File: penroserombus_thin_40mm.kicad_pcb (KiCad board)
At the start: 2 copper layers, 72.4 x 23.5 mm, 15 parts, among them J1 Conn_01x03_Female, J2 Conn_01x03_Female, J3 Conn_01x03_Male, J4 Conn_01x03_Male, M2 MountingHole_2.2mm_M2_ISO7380, SW1 SW_DPDT_x2

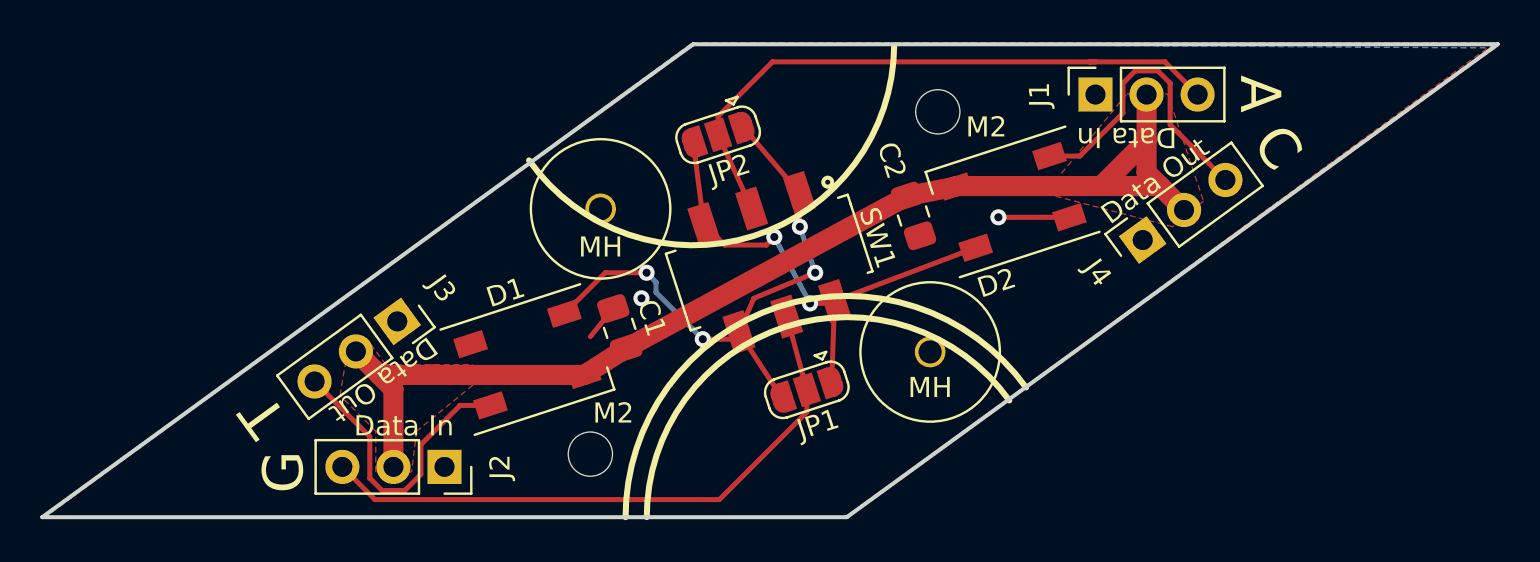
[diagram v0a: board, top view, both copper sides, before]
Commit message: board has 4 leds instead of 2.
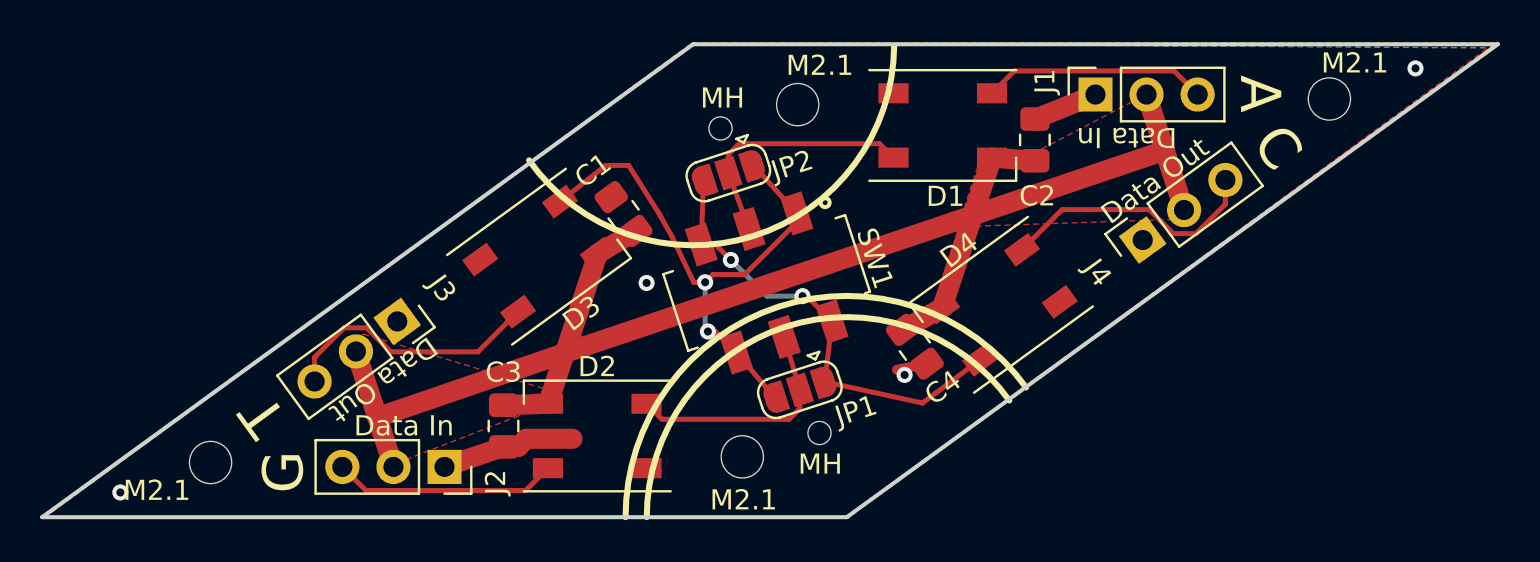
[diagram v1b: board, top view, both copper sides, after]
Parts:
- removed M2 (x2): MountingHole_2.2mm_M2_ISO7380, MountingHole:MountingHole_2.2mm_M2_ISO7380
- removed the MH at (162.9, 76.8)
- removed the MH at (146.6, 69.7)
- added C3: C, Capacitor_SMD:C_0805_2012Metric_Pad1.18x1.45mm_HandSolder, F.Cu at (141.7, 80.5)
- added C4: C, Capacitor_SMD:C_0805_2012Metric_Pad1.18x1.45mm_HandSolder, F.Cu at (162.2, 76.6)
- added D1: SK6812, LED_SMD:LED_SK6812_PLCC4_5.0x5.0mm_P3.2mm, F.Cu at (163.6, 65.6)
- added D2: SK6812, LED_SMD:LED_SK6812_PLCC4_5.0x5.0mm_P3.2mm, F.Cu at (146.4, 81.0)
- added M2.1: MountingHole_2.1mm, MountingHole:MountingHole_2.1mm, F.Cu at (153.6, 82.1)
- added M2.1: MountingHole_2.1mm, MountingHole:MountingHole_2.1mm, F.Cu at (156.4, 64.5)
- added M2.1: MountingHole_2.1mm, MountingHole:MountingHole_2.1mm, F.Cu at (127.2, 82.3)
- added M2.1: MountingHole_2.1mm, MountingHole:MountingHole_2.1mm, F.Cu at (182.8, 64.3)
- added MH: Pushpin_mountinghole, penroserombus:Pushpin_mountinghole, F.Cu at (157.4, 80.9)
- added MH: Pushpin_mountinghole, penroserombus:Pushpin_mountinghole, F.Cu at (152.5, 65.7)
- moved C2 7.12 mm to (168.1, 66.3), turned to 270 degrees
- moved C1 5.69 mm to (147.7, 70.0), turned to 306 degrees
- moved D3 5.15 mm to (143.5, 72.1), turned to 36 degrees
- moved D4 5.15 mm to (166.5, 74.5), turned to 216 degrees
- moved JP2 1.97 mm to (152.9, 67.9)
- moved SW1 1.02 mm to (154.8, 73.4)
- moved JP1 0.35 mm to (156.5, 78.7)
- renumbered D1 to D3, D2 to D4
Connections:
- J1 pad 3: Net-(J1-Pad3) -> Net-(D1-Pad2)
- J2 pad 3: Net-(J2-Pad3) -> Net-(D2-Pad2)
- JP1 pad 2: Net-(J2-Pad3) -> Net-(D2-Pad4)
- JP2 pad 2: Net-(J1-Pad3) -> Net-(D1-Pad4)
- SW1 pad 2: Net-(J1-Pad3) -> Net-(D1-Pad4)
- SW1 pad 5: Net-(J2-Pad3) -> Net-(D2-Pad4)
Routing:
- net Net-(J1-Pad3): track 30.9 -> 0.00 mm
- net Net-(J2-Pad3): track 30.4 -> 0.00 mm
- net VCC: track 57.4 -> 77.9 mm
- net Net-(D1-Pad4): track 0.00 -> 12.6 mm
- net Net-(D2-Pad4): track 0.00 -> 11.8 mm
- net Net-(D1-Pad2): track 0.00 -> 11.2 mm
- net Net-(D2-Pad2): track 0.00 -> 11.2 mm
- net GND: track 5.37 -> 11.5 mm, vias 2 -> 4
- net Net-(D4-Pad2): track 24.9 -> 22.8 mm
- net Net-(D3-Pad4): track 14.9 -> 13.2 mm
- net Net-(D4-Pad4): track 14.8 -> 13.2 mm
- net Net-(D3-Pad2): track 29.2 -> 28.1 mm, vias 4 -> 2

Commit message: small tweaks to traces
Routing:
- net GND: vias 4 -> 11
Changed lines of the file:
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@@
     (thickness 1.6)
     (drawings 31)
-    (tracks 82)
+    (tracks 90)
     (zones 0)
     (modules 21)
@@
       (effects (font (size 0.5 0.5) (thickness 0.08)))
     )
-    (pad 1 smd roundrect (at -1.0375 0 126) (size 1.175 1.45) (layers F.Cu F.Paste F.Mask) (roundrect_rratio 0.212766)
-      (net 2 GND))
-    (pad 2 smd roundrect (at 1.0375 0 126) (size 1.175 1.45) (layers F.Cu F.Paste F.Mask) (roundrect_rratio 0.212766)
+    (pad 1 smd roundrect (at -1.0375 0 126) (size 1.175 1.45) (layers F.Cu F.Paste F.Mask) (roundrect_rratio 0.2127659574468085)
+      (net 2 GND))
+    (pad 2 smd roundrect (at 1.0375 0 126) (size 1.175 1.45) (layers F.Cu F.Paste F.Mask) (roundrect_rratio 0.2127659574468085)
       (net 1 VCC))
     (model ${KISYS3DMOD}/Capacitor_SMD.3dshapes/C_0805_2012Metric.wrl
@@
       (effects (font (size 0.5 0.5) (thickness 0.08)))
     )
-    (pad 2 smd roundrect (at 1.0375 0 90) (size 1.175 1.45) (layers F.Cu F.Paste F.Mask) (roundrect_rratio 0.212766)
-      (net 1 VCC))
-    (pad 1 smd roundrect (at -1.0375 0 90) (size 1.175 1.45) (layers F.Cu F.Paste F.Mask) (roundrect_rratio 0.212766)
+    (pad 2 smd roundrect (at 1.0375 0 90) (size 1.175 1.45) (layers F.Cu F.Paste F.Mask) (roundrect_rratio 0.2127659574468085)
+      (net 1 VCC))
+    (pad 1 smd roundrect (at -1.0375 0 90) (size 1.175 1.45) (layers F.Cu F.Paste F.Mask) (roundrect_rratio 0.2127659574468085)
       (net 2 GND))
     (model ${KISYS3DMOD}/Capacitor_SMD.3dshapes/C_0805_2012Metric.wrl
@@
   (segment (start 142.457 81.5555) (end 142.8595 81.153) (width 1) (layer F.Cu) (net 2))
   (segment (start 141.732 81.5555) (end 142.457 81.5555) (width 1) (layer F.Cu) (net 2))
-  (segment (start 142.8595 81.153) (end 145.161 81.153) (width 1) (layer F.Cu) (net 2))
+  (segment (start 142.8595 81.153) (end 143.129 81.153) (width 1) (layer F.Cu) (net 2))
   (segment (start 138.799045 82.55) (end 141.732 81.5555) (width 1) (layer F.Cu) (net 2))
-  (via (at 161.671 77.978) (size 0.8) (drill 0.4) (layers F.Cu B.Cu) (net 2))
+  (via (at 164.211 76.2) (size 0.8) (drill 0.4) (layers F.Cu B.Cu) (net 2))
   (segment (start 162.788827 77.420355) (end 161.29 77.724) (width 0.5) (layer F.Cu) (net 2))
   (segment (start 171.159724 64.03859) (end 168.148 65.2565) (width 1) (layer F.Cu) (net 2))
+  (via (at 162.814 64.008) (size 0.8) (drill 0.4) (layers F.Cu B.Cu) (net 2))
+  (via (at 166.37 65.405) (size 0.8) (drill 0.4) (layers F.Cu B.Cu) (net 2))
+  (via (at 168.021 75.438) (size 0.8) (drill 0.4) (layers F.Cu B.Cu) (net 2))
+  (segment (start 143.129 81.153) (end 145.161 81.153) (width 1) (layer F.Cu) (net 2))
+  (via (at 143.129 81.153) (size 0.8) (drill 0.4) (layers F.Cu B.Cu) (net 2))
+  (via (at 147.193 82.55) (size 0.8) (drill 0.4) (layers F.Cu B.Cu) (net 2))
+  (via (at 141.986 71.247) (size 0.8) (drill 0.4) (layers F.Cu B.Cu) (net 2))
+  (via (at 145.796 70.231) (size 0.8) (drill 0.4) (layers F.Cu B.Cu) (net 2))
   (segment (start 175.064723 62.863589) (end 176.239724 64.03859) (width 0.25) (layer F.Cu) (net 3))
   (segment (start 167.128832 62.863589) (end 175.064723 62.863589) (width 0.25) (layer F.Cu) (net 3))

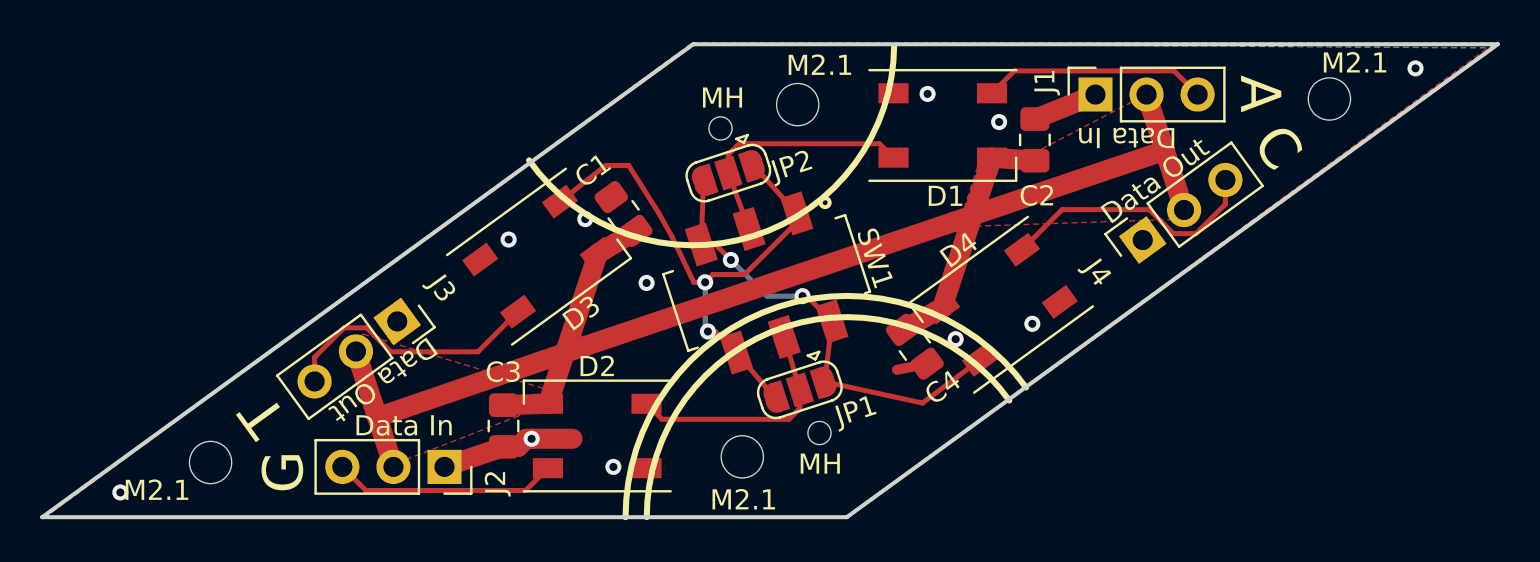
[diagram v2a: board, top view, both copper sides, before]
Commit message: shifted ports  on penrose rhombi to enforce all matching rules. fixed flipped ports on penrose dart.
going to make new gerbers later.
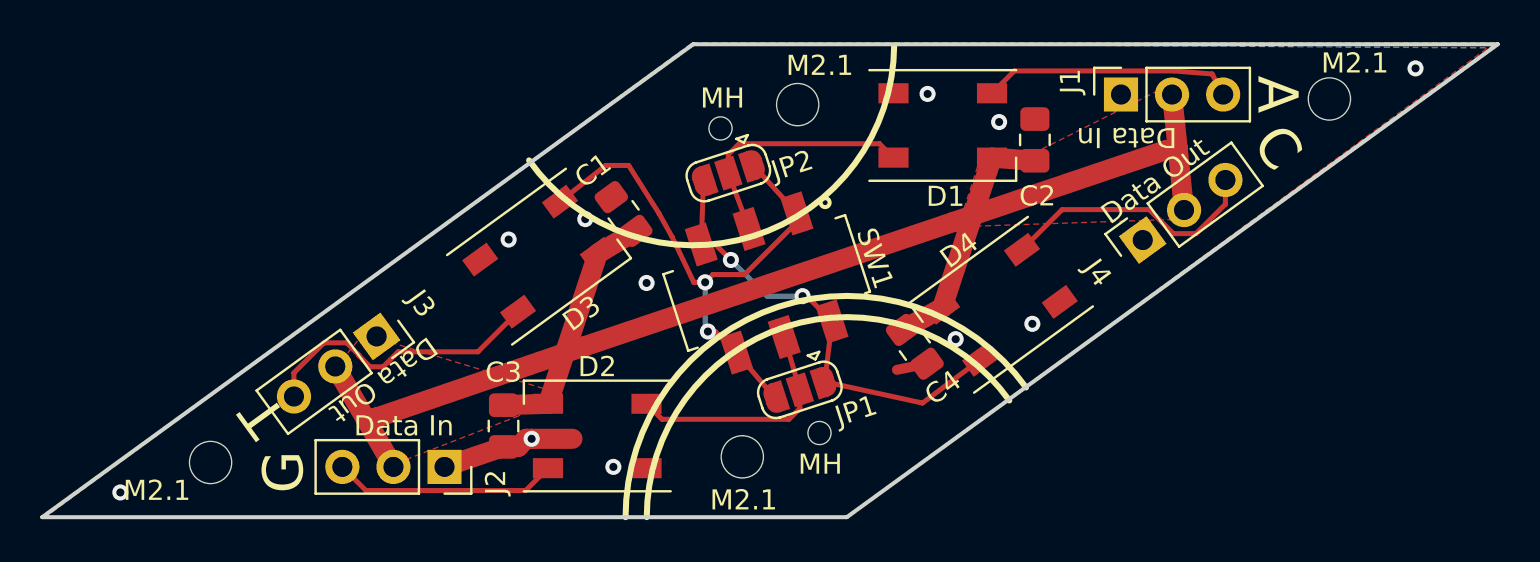
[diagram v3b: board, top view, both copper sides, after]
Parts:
- moved J3 1.27 mm to (135.4, 76.1)
- moved J1 1.27 mm to (172.4, 64.0)
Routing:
- net GND: track 11.5 -> 8.22 mm
- net Net-(D1-Pad2): track 11.2 -> 12.6 mm
- net Net-(D3-Pad4): track 13.2 -> 14.6 mm
- net VCC: track 77.9 -> 78.6 mm
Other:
- board text added: "Gnd Vcc Data"
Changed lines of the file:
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@@
   (general
     (thickness 1.6)
-    (drawings 31)
-    (tracks 90)
+    (drawings 33)
+    (tracks 95)
     (zones 0)
     (modules 21)
@@
     )
   )
-  (module Connector_PinSocket_2.54mm:PinSocket_1x03_P2.54mm_Vertical locked (layer F.Cu)
-    (at 136.448848 75.316838 306)
+  (module Connector_PinSocket_2.54mm:PinSocket_1x03_P2.54mm_Vertical (layer F.Cu)
+    (at 135.422873 76.063088 306)
     (descr "Through hole straight socket strip, 1x03, 2.54mm pitch, single row (from Kicad 4.0.7), script generated")
     (tags "Through hole socket strip THT 1x03 2.54mm single row")
@@
     )
   )
-  (module Connector_PinSocket_2.54mm:PinSocket_1x03_P2.54mm_Vertical locked (layer F.Cu)
-    (at 171.159724 64.03859 90)
+  (module Connector_PinSocket_2.54mm:PinSocket_1x03_P2.54mm_Vertical (layer F.Cu)
+    (at 172.428389 64.039267 90)
     (descr "Through hole straight socket strip, 1x03, 2.54mm pitch, single row (from Kicad 4.0.7), script generated")
     (tags "Through hole socket strip THT 1x03 2.54mm single row")
@@
       (net 4 "Net-(D1-Pad4)"))
   )
+  (gr_text "Gnd\nVcc\nData" (at 136.0678 80.9498 288) (layer B.SilkS)
+    (effects (font (size 1.5 0.8) (thickness 0.2)) (justify left mirror))
+  )
+  (gr_text "Gnd\nVcc\nData" (at 173.3804 65.8368 108) (layer B.SilkS)
+    (effects (font (size 1.5 0.8) (thickness 0.2)) (justify left mirror))
+  )
   (gr_text "Data Out" (at 135.763 78.232 216) (layer F.SilkS)
     (effects (font (size 1 1) (thickness 0.15)))
@@
     (effects (font (size 2 2) (thickness 0.5)))
   )
-  (gr_text A (at 179.324 64.008 270) (layer F.SilkS)
+  (gr_text A (at 180.1876 64.0334 270) (layer F.SilkS)
     (effects (font (size 2 2) (thickness 0.5)))
   )
@@
   (gr_line (start 151.159725 61.538591) (end 118.799045 85.05) (layer Edge.Cuts) (width 0.2))
   (segment (start 164.098273 70.372273) (end 145.766591 76.551591) (width 1) (layer F.Cu) (net 1))
-  (segment (start 174.604327 66.822673) (end 175.564824 69.778778) (width 1) (layer F.Cu) (net 1))
   (segment (start 164.098273 70.372273) (end 174.604327 66.822673) (width 1) (layer F.Cu) (net 1))
-  (segment (start 173.699724 64.03859) (end 174.604327 66.822673) (width 1) (layer F.Cu) (net 1))
-  (segment (start 134.393945 76.809813) (end 135.234187 79.395813) (width 1) (layer F.Cu) (net 1))
-  (segment (start 135.458655 80.086655) (end 136.259045 82.55) (width 1) (layer F.Cu) (net 1))
   (segment (start 145.766591 76.551591) (end 135.458655 80.086655) (width 1) (layer F.Cu) (net 1))
-  (segment (start 135.234187 79.395813) (end 135.458655 80.086655) (width 1) (layer F.Cu) (net 1))
   (segment (start 141.732 79.4805) (end 143.942394 79.412545) (width 1) (layer F.Cu) (net 1))
   (segment (start 143.942394 79.412545) (end 146.418238 71.95176) (width 1) (layer F.Cu) (net 1))
@@
   (segment (start 163.540531 74.63683) (end 166.016375 67.176046) (width 1) (layer F.Cu) (net 1))
   (segment (start 166.016375 67.176046) (end 168.148 67.3315) (width 1) (layer F.Cu) (net 1))
+  (segment (start 174.604327 66.822673) (end 175.246345 66.714055) (width 1) (layer F.Cu) (net 1))
+  (segment (start 175.246345 66.714055) (end 175.564824 69.778778) (width 1) (layer F.Cu) (net 1))
+  (segment (start 174.968389 64.039267) (end 175.246345 66.714055) (width 1) (layer F.Cu) (net 1))
+  (segment (start 135.458655 80.086655) (end 134.8851 80.1767) (width 1) (layer F.Cu) (net 1))
+  (segment (start 134.8851 80.1767) (end 133.36797 77.556063) (width 1) (layer F.Cu) (net 1))
+  (segment (start 136.259045 82.55) (end 134.8851 80.1767) (width 1) (layer F.Cu) (net 1))
   (via (at 187.071 62.738) (size 0.8) (drill 0.4) (layers F.Cu B.Cu) (net 2))
   (via (at 122.682 83.82) (size 0.8) (drill 0.4) (layers F.Cu B.Cu) (net 2))
@@
   (via (at 164.211 76.2) (size 0.8) (drill 0.4) (layers F.Cu B.Cu) (net 2))
   (segment (start 162.788827 77.420355) (end 161.29 77.724) (width 0.5) (layer F.Cu) (net 2))
-  (segment (start 171.159724 64.03859) (end 168.148 65.2565) (width 1) (layer F.Cu) (net 2))
   (via (at 162.814 64.008) (size 0.8) (drill 0.4) (layers F.Cu B.Cu) (net 2))
   (via (at 166.37 65.405) (size 0.8) (drill 0.4) (layers F.Cu B.Cu) (net 2))
@@
   (via (at 141.986 71.247) (size 0.8) (drill 0.4) (layers F.Cu B.Cu) (net 2))
   (via (at 145.796 70.231) (size 0.8) (drill 0.4) (layers F.Cu B.Cu) (net 2))
-  (segment (start 175.064723 62.863589) (end 176.239724 64.03859) (width 0.25) (layer F.Cu) (net 3))
   (segment (start 167.128832 62.863589) (end 175.064723 62.863589) (width 0.25) (layer F.Cu) (net 3))
   (segment (start 166.016375 63.976046) (end 167.128832 62.863589) (width 0.25) (layer F.Cu) (net 3))
+  (segment (start 175.064723 62.863589) (end 176.9618 63.0174) (width 0.25) (layer F.Cu) (net 3))
+  (segment (start 176.9618 63.0174) (end 177.508389 64.039267) (width 0.25) (layer F.Cu) (net 3))
   (segment (start 152.908 67.945) (end 153.940027 70.719265) (width 0.25) (layer F.Cu) (net 4))
   (segment (start 160.42093 66.480601) (end 161.116375 67.176046) (width 0.25) (layer F.Cu) (net 4))
@@
   (segment (start 149.468305 69.963713) (end 150.114 71.12) (width 0.25) (layer F.Cu) (net 7))
   (segment (start 150.114 71.12) (end 151.190273 73.371857) (width 0.25) (layer F.Cu) (net 7))
-  (segment (start 136.126176 76.82913) (end 140.456833 76.82913) (width 0.25) (layer F.Cu) (net 8))
   (segment (start 140.456833 76.82913) (end 142.454055 74.831908) (width 0.25) (layer F.Cu) (net 8))
-  (segment (start 133.804936 75.634812) (end 134.931858 75.634812) (width 0.25) (layer F.Cu) (net 8))
-  (segment (start 132.339042 77.100706) (end 133.804936 75.634812) (width 0.25) (layer F.Cu) (net 8))
-  (segment (start 134.931858 75.634812) (end 136.126176 76.82913) (width 0.25) (layer F.Cu) (net 8))
-  (segment (start 132.339042 78.302787) (end 132.339042 77.100706) (width 0.25) (layer F.Cu) (net 8))
+  (segment (start 131.313067 77.871964) (end 131.313067 79.049037) (width 0.25) (layer F.Cu) (net 8))
+  (segment (start 132.803969 76.381062) (end 131.313067 77.871964) (width 0.25) (layer F.Cu) (net 8))
+  (segment (start 133.931971 76.381062) (end 132.803969 76.381062) (width 0.25) (layer F.Cu) (net 8))
+  (segment (start 134.542971 76.992062) (end 133.931971 76.381062) (width 0.25) (layer F.Cu) (net 8))
+  (segment (start 136.491795 76.82913) (end 135.745545 77.57538) (width 0.25) (layer F.Cu) (net 8))
+  (segment (start 140.456833 76.82913) (end 136.491795 76.82913) (width 0.25) (layer F.Cu) (net 8))
+  (segment (start 134.542971 77.019531) (end 135.09882 77.57538) (width 0.25) (layer F.Cu) (net 8))
+  (segment (start 134.542971 76.992062) (end 134.542971 77.019531) (width 0.25) (layer F.Cu) (net 8))
+  (segment (start 135.745545 77.57538) (end 135.09882 77.57538) (width 0.25) (layer F.Cu) (net 8))
   (segment (start 173.832593 69.759461) (end 169.501935 69.759461) (width 0.25) (layer F.Cu) (net 9))
   (segment (start 175.026911 70.953779) (end 173.832593 69.759461) (width 0.25) (layer F.Cu) (net 9))
@@
     (polygon
       (pts
-        (xy 144.018 78.74) (xy 142.494 80.01) (xy 136.271 82.423) (xy 134.366 76.327) (xy 134.747 75.946)
+        (xy 144.018 78.74) (xy 142.494 80.01) (xy 136.271 82.423) (xy 133.096 78.0034) (xy 134.747 75.946)
       )
     )
@@
     (polygon
       (pts
-        (xy 175.514 70.231) (xy 164.338 70.612) (xy 165.481 67.056) (xy 167.64 67.183) (xy 173.736 64.008)
+        (xy 175.514 70.231) (xy 164.338 70.612) (xy 165.481 67.056) (xy 167.64 67.183) (xy 174.8028 63.5762)
       )
     )
